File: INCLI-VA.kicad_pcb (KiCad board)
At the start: 2 copper layers, 100 x 100 mm, 167 parts, among them J1 MSTBV 2,5/5-GF-5,08, J2 MSTBV 2,5/2-GF-5,08, J401 USB4105-GF-A, J402 UART0, Q101 STD18NF25, Q102 IPD30N10S3L-34, Q701 DMN10H220LQ, Q751 DMN10H220LQ, SW401 RESET, SW402 BOOT, U101 LM74930QRGERQ1, U201 LMR38010SQDDARQ1, U301 TPS62A02QDRLRQ1, U302 LP5907QMFX-3.3Q1, U401 ESP32-S3-WROOM-1-N8R2, U402 USBLC6-2SC6, U501 SCL3300-D01, U502 ASM330LHHTR, U503 AS5147U-HTSM, U601 ADM3055E, U701 74AHCT1G126, U751 74AHCT1G126, U801 TPS3828-33Q1

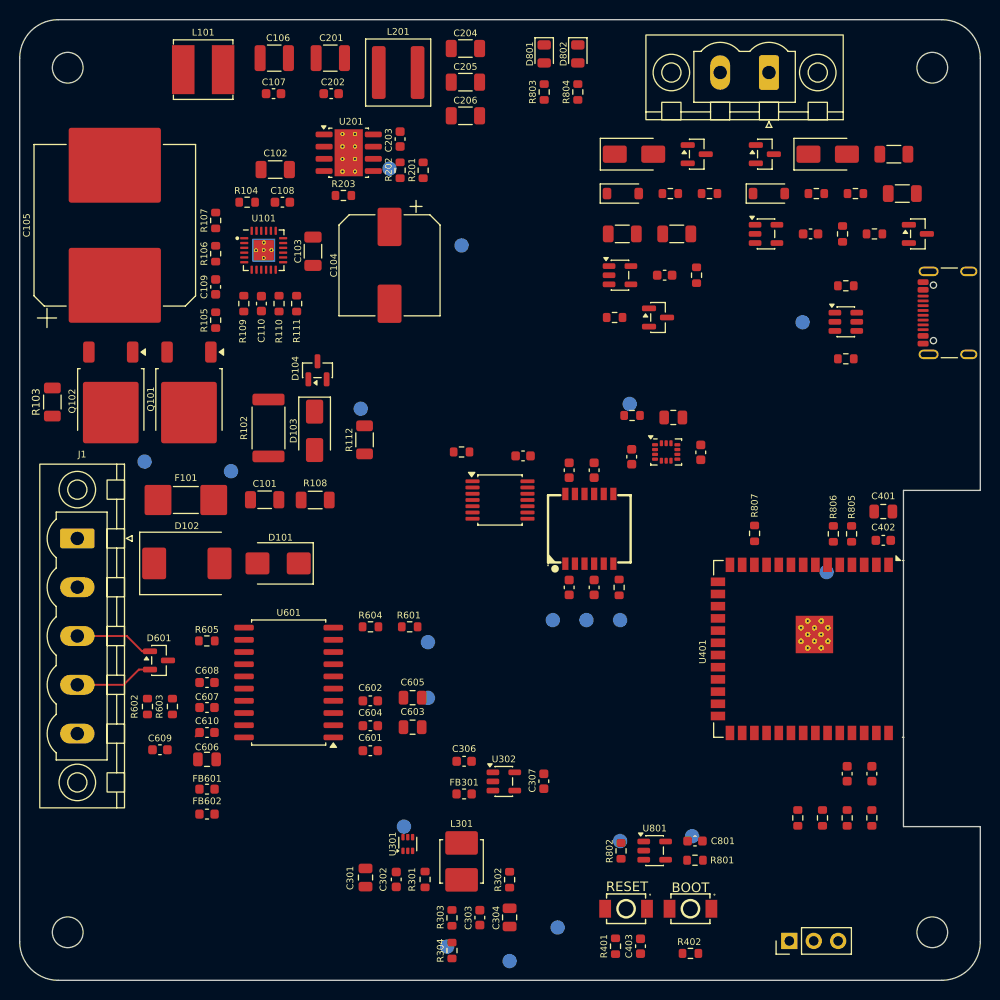
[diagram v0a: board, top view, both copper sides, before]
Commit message: [Claude Code] PCB: C403 al EN, lazos del buck, J401 al borde, courtyards y referencias 0.8 mm
- C403 a 1.3 mm del pin EN de U401; C202 a 1.06 mm de VIN/GND de U201;
  C204-C206 en columna junto a C203; J401 -0.4 mm (sin errores de borde)
- Courtyards: solo C403-C402 queda bajo criterio (0.7 mm)
- Referencias 0.8/0.8/0.15 a 0/90 grados; regla JLC_serigrafia 0.8/0.15
- DRC 0 errores, paridad 0, sin ruteo

Co-Authored-By: Claude Opus 5.5 <noreply@anthropic.com>
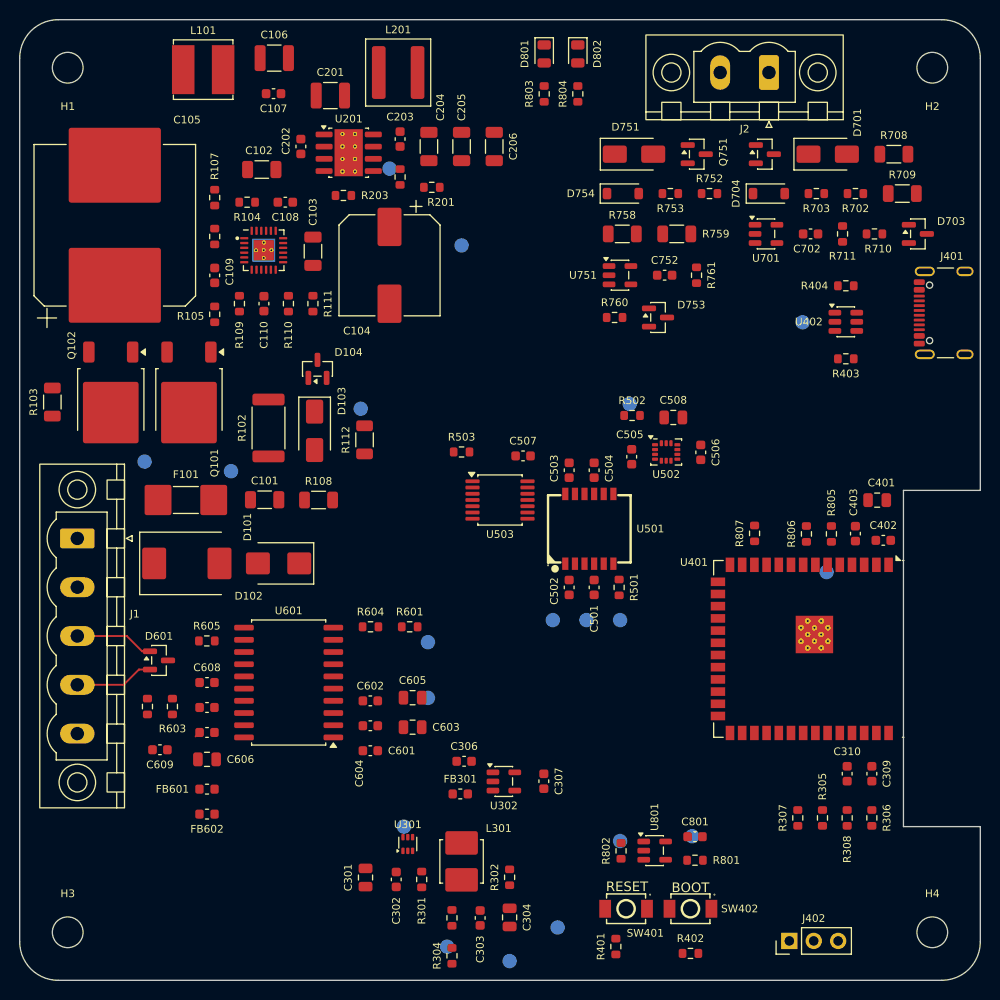
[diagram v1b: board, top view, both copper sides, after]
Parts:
- moved C403 48.4 mm to (187.0, 103.5), turned to 90 degrees
- moved C204 10.9 mm to (142.6, 63.2), turned to -90 degrees
- moved C205 6.71 mm to (146.0, 63.2), turned to -90 degrees
- moved C202 6.34 mm to (129.3, 63.2), turned to 90 degrees
- moved C206 4.38 mm to (149.4, 63.2), turned to -90 degrees
- moved C201 3.90 mm to (132.3, 57.9)
- moved R806 2.80 mm to (181.9, 103.5)
- moved R107 2.38 mm to (120.3, 68.5)
- moved R805 2.10 mm to (184.5, 103.5)
- moved R201 1.99 mm to (142.9, 67.5), turned to 180 degrees
- moved R106 1.79 mm to (120.3, 72.6)
- moved R111 1.70 mm to (130.5, 79.6)
- moved C102 1.40 mm to (125.2, 65.6)
- moved C401 1.35 mm to (189.3, 100.0)
- moved C109 1.20 mm to (120.3, 76.6)
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
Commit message: [Claude Code] PCB: H1-H5 M3 metalizados sin red, apoyo B, barrera CAN, pinout y nombre en serigrafia
- H1-H4 a MountingHole_3.2mm_M3_Pad y H5 nuevo en (56.0, 38.5); simbolo sin pin,
  anillo flotante. Reglas H_anillo_cobre (0.5 mm) y H_zona_arandela (4 mm del centro).
- Rule area APOYO_CAJA_B (8 mm en B.Cu, 63.5/49.0): sin pistas/vias/pads, relleno permitido.
- Serigrafia 0.8/0.15: linea de barrera CAN y "CAN AISLADO" en ambas caras, pinout J1/J2,
  nombre/Rev/fecha abajo, rotulos de zona. Incluye el borrado de CAN_H/CAN_L del usuario.
- DRC 0 errores, paridad 0; ERC 0 errores; sch_visual_qa raiz PASS. Sin ruteo.

Co-Authored-By: Claude Opus 5.5 <noreply@anthropic.com>
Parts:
- added H5: MountingHole_M3, MountingHole:MountingHole_3.2mm_M3_Pad, F.Cu at (156.0, 88.5)
- H1, H2, H3, H4: footprint MountingHole:MountingHole_3.2mm_M3 -> MountingHole:MountingHole_3.2mm_M3_Pad
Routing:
- net /BUS_CAN_L: track 8.22 -> 0.00 mm
- net /BUS_CAN_H: track 8.22 -> 0.82 mm
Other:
- board text added: "BUCK 5V"
- board text added: "CAN AISLADO"
- board text added: "CANH"
- board text added: "CANL"
- board text added: "DO1"
- board text added: "DO2"
- board text added: "ENTRADA"
- board text added: "GND"
- board text added: "GND_CAN"
- board text added: "INCLI-VA Rev A 2026-10-29"
- board text added: "SALIDAS DO"
- board text added: "SENSORES"
- board text added: "VIN"
